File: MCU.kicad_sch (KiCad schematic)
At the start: 1 part, among them U1 STM32F103RET6TR

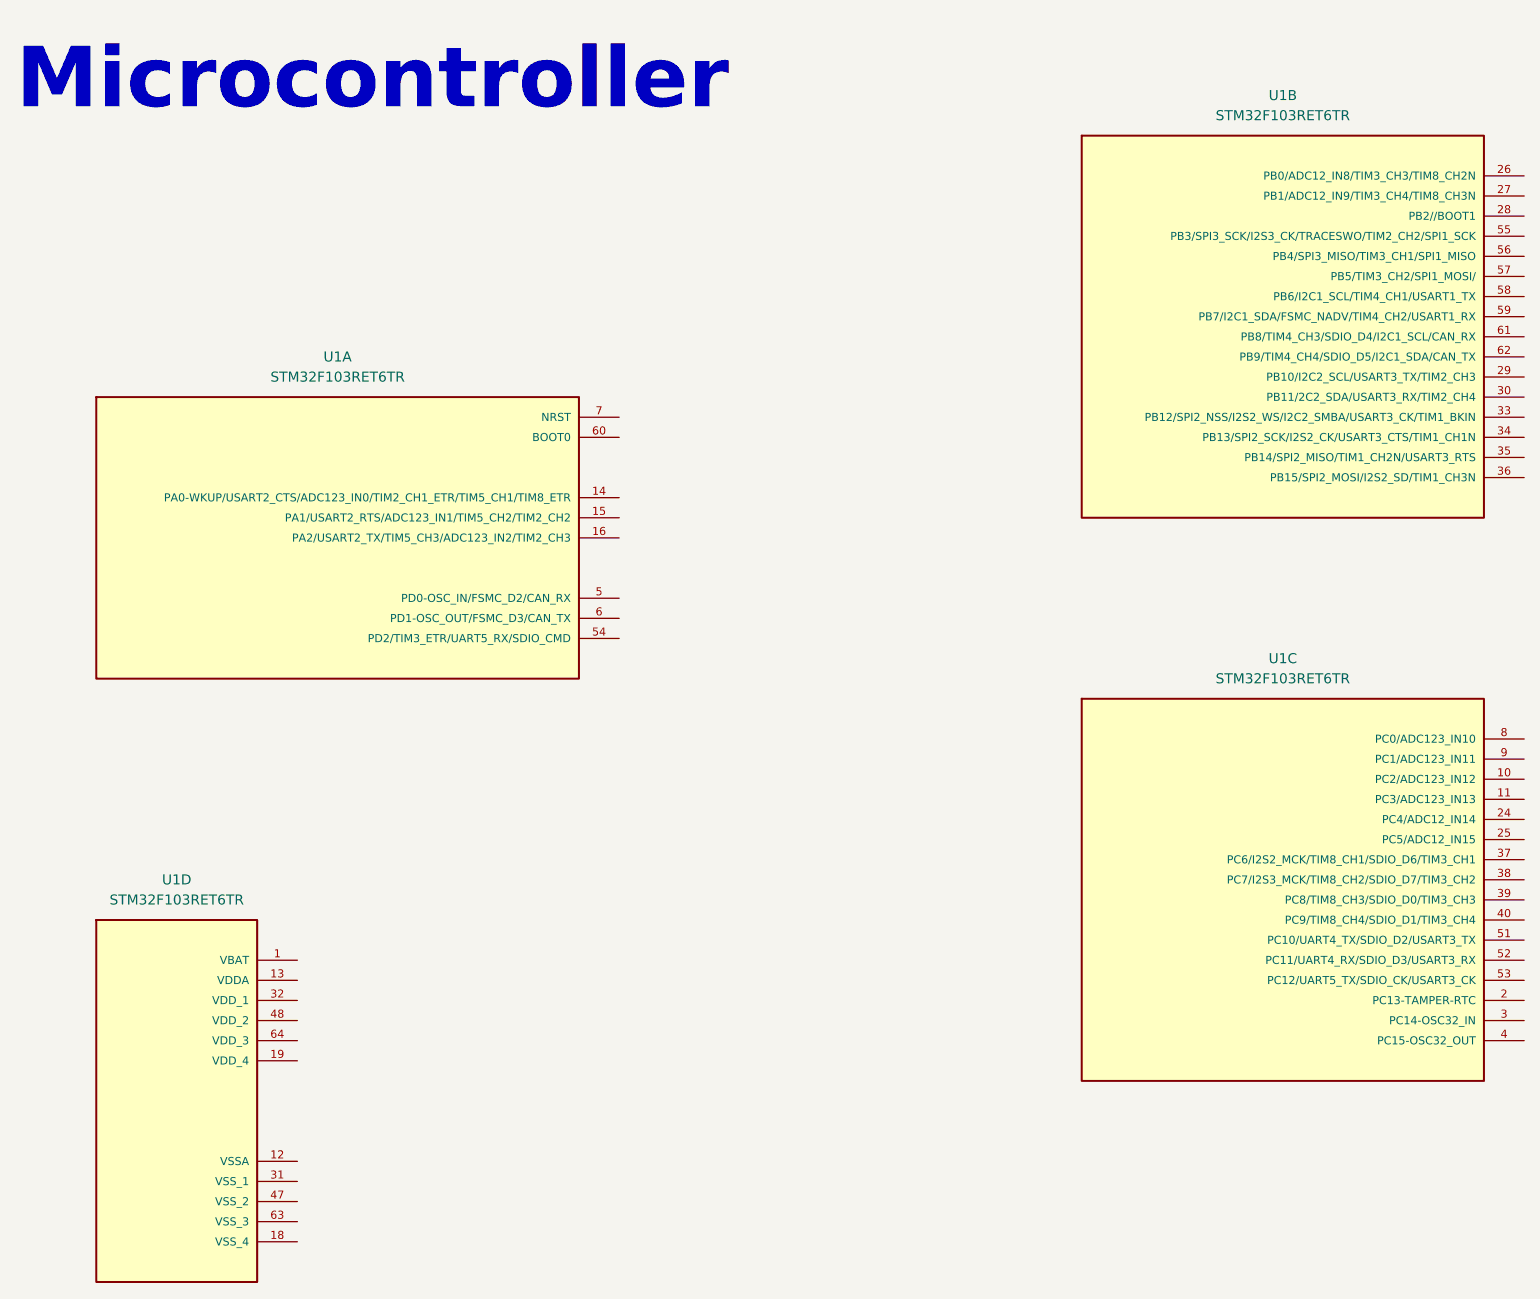
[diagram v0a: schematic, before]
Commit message: Worked more on CODEC sheet, beginning symbol for new MCU part chosen
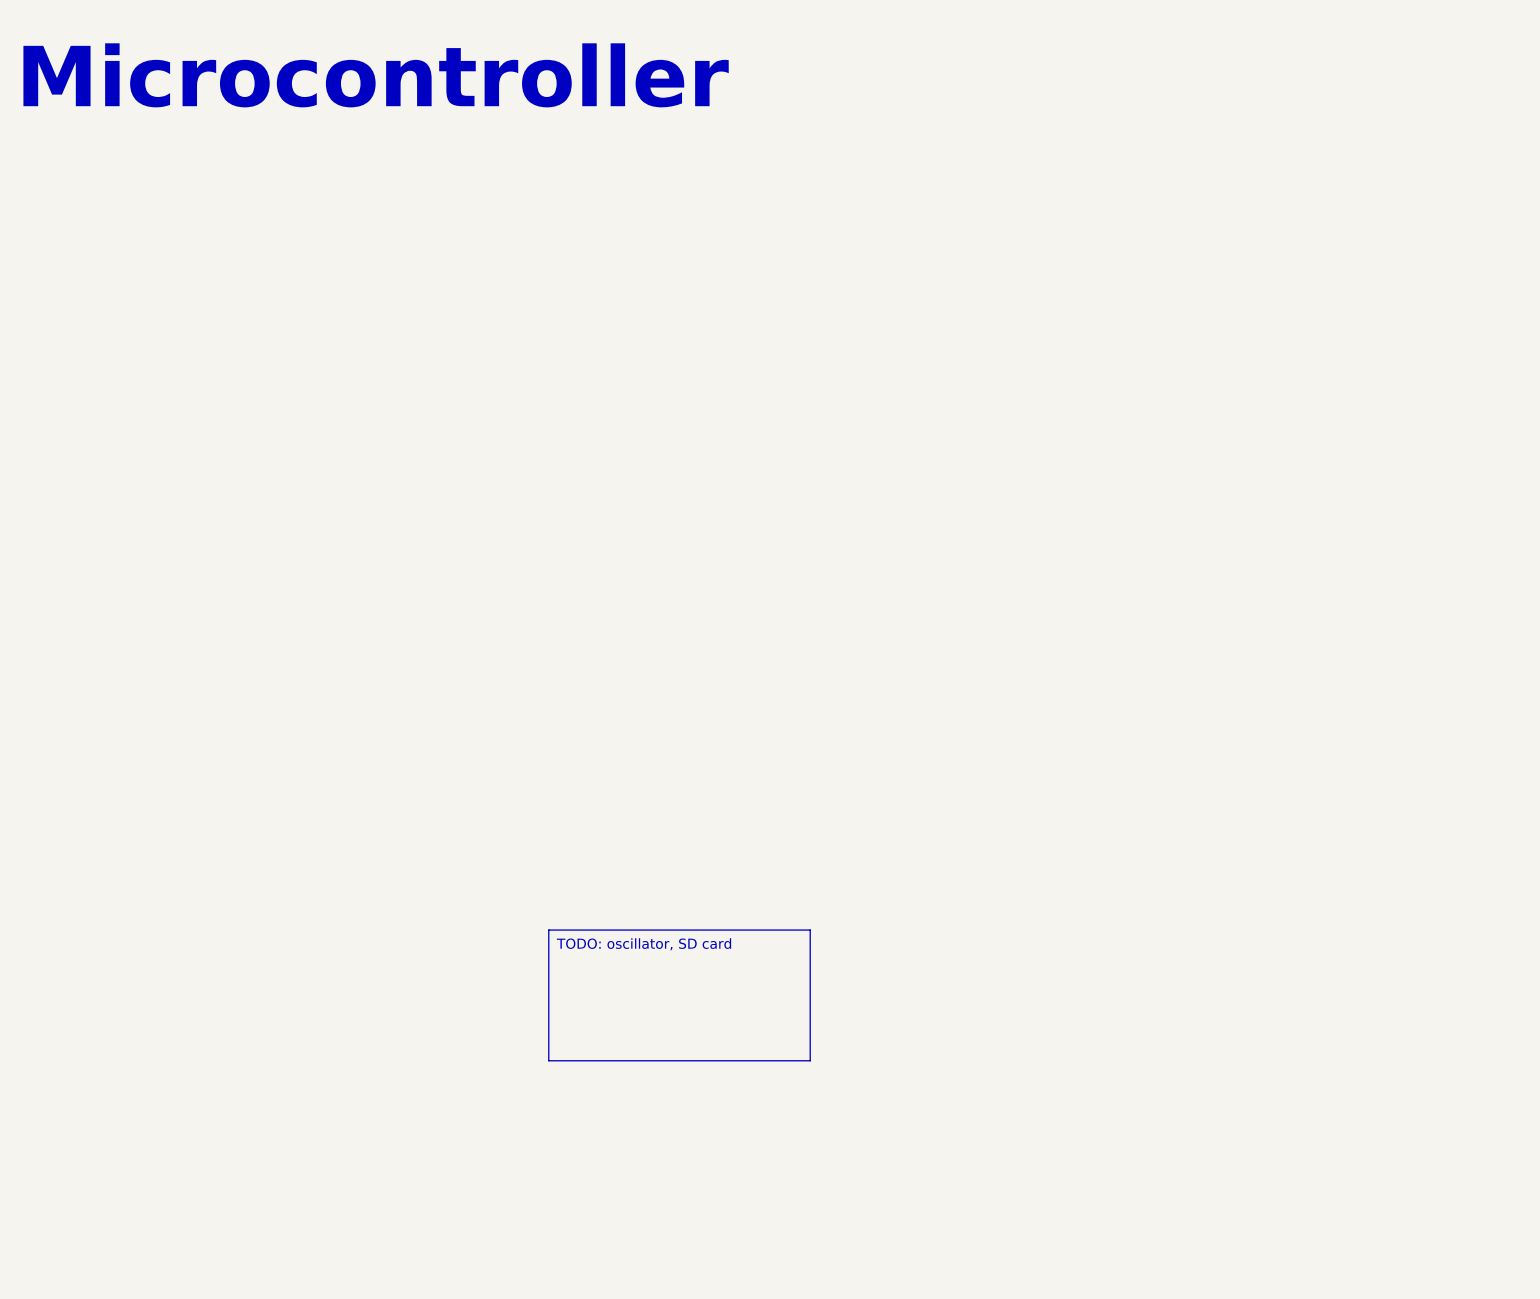
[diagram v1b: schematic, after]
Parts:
- removed U1: STM32F103RET6TR, STM32:QFP50P1200X1200X160-64N, symbol STM32:STM32F103RET6TR
